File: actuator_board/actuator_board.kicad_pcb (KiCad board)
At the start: 2 copper layers, 26.7 x 37.1 mm, 28 parts, among them J1 Conn_01x10_Socket, J2 Conn_01x02_Socket, Q1 Q_NMOS_GSD, Q2 Q_NMOS_GSD, Q3 Q_NMOS_GSD, Q4 Q_NMOS_GSD, Q5 Q_NMOS_GSD, U1 113991054, U8 STLQ015M33R

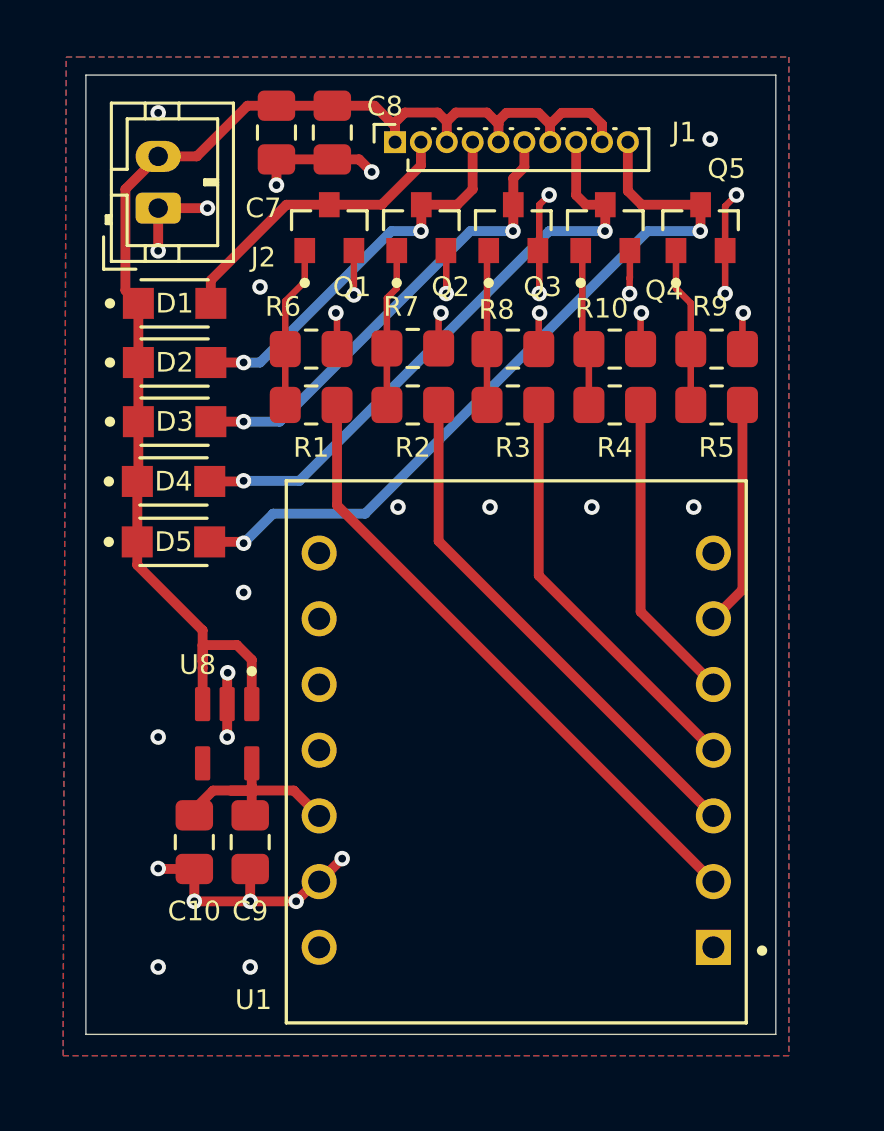
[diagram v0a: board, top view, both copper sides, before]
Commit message: Fixed actuator board and revised magnetometer board
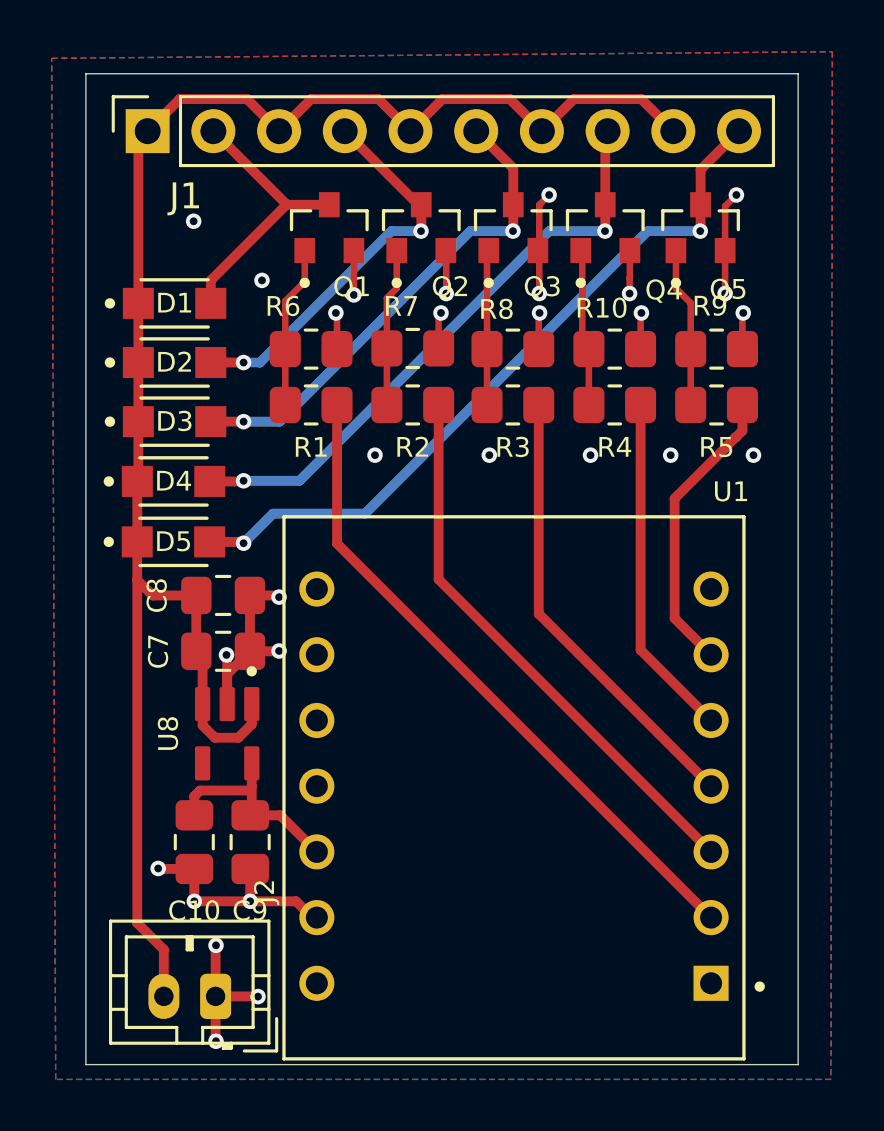
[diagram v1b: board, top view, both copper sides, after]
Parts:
- J1: footprint Connector_PinSocket_1.00mm:PinSocket_1x10_P1.00mm_Vertical -> Connector_PinSocket_2.54mm:PinSocket_1x10_P2.54mm_Vertical
- moved J2 30.6 mm to (134.3, 112.0), turned to 180 degrees
- moved C7 20.2 mm to (134.6, 98.7), turned to 0 degrees
- moved C8 18.4 mm to (134.6, 96.5), turned to 0 degrees
- moved J1 9.57 mm to (131.7, 78.6)
- moved U1 1.39 mm to (145.8, 103.9)
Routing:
- net +V_{BATT}: track 51.4 -> 69.8 mm
- net Net-(U1-D5): track 8.73 -> 11.3 mm
- net GND: track 41.3 -> 43.1 mm, vias 34 -> 28
- net /MOTOR5-: track 29.9 -> 28.5 mm
- net Net-(U1-D3): track 16.1 -> 17.5 mm
- net Net-(U1-D2): track 20.3 -> 21.6 mm
- net Net-(U1-D1): track 24.5 -> 25.8 mm
- net Net-(U1-D4): track 12.0 -> 13.3 mm
- net /MOTOR1-: track 11.8 -> 10.7 mm
- net /MOTOR3-: track 18.4 -> 19.2 mm
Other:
- board size 26.7 x 37.1 mm -> 27.5 x 38.3 mm

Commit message: updates
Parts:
- moved J2 0.15 mm to (134.1, 112.0)
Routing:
- net GND: track 43.1 -> 42.0 mm, vias 28 -> 32
- net /MOTOR2-: track 15.4 -> 16.3 mm

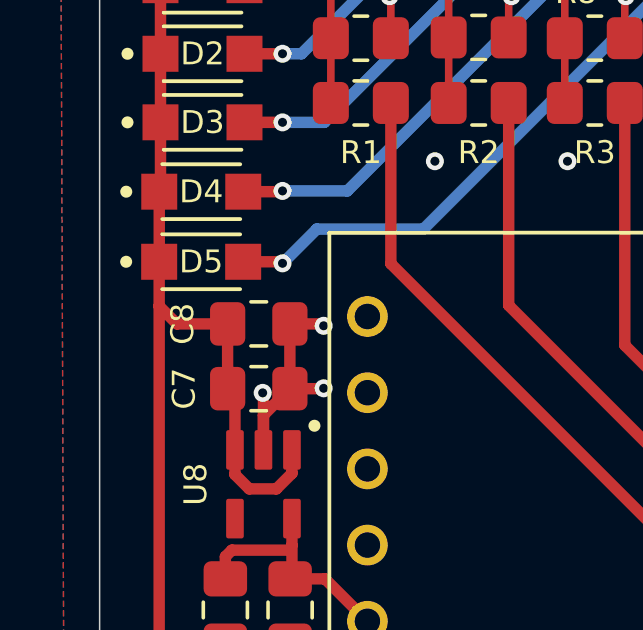
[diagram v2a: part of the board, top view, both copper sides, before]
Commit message: Re-layout of sensor control board
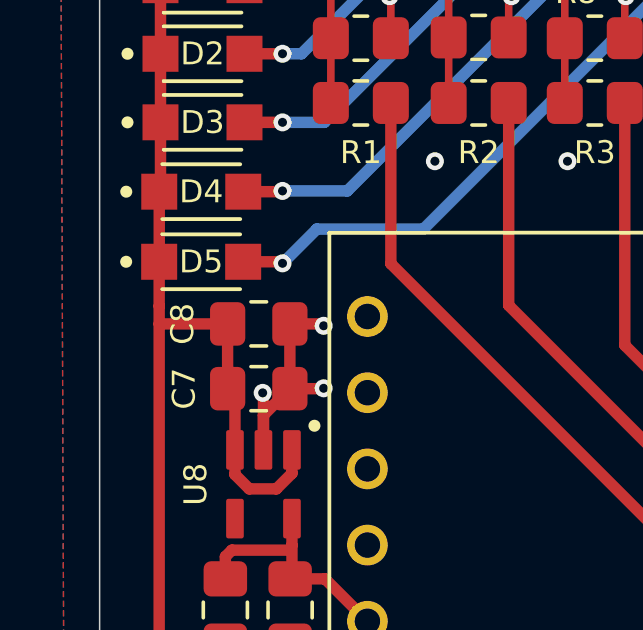
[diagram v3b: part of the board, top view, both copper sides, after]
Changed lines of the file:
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@@
+	)
+	(segment
+		(start 131.2705 96.5073)
+		(end 133.5532 96.5073)
+		(width 0.381)
+		(layer "F.Cu")
+		(net 2)
 	)
 	(segment
@@
 	)
 	(segment
-		(start 131.2705 95.9137)
-		(end 131.8641 96.5073)
-		(width 0.381)
-		(layer "F.Cu")
-		(net 2)
-	)
-	(segment
 		(start 134.273908 102.0064)
 		(end 133.797 101.529492)
@@
 		(width 0.381)
 		(layer "F.Cu")
-		(net 2)
-	)
-	(segment
-		(start 131.8641 96.5073)
-		(end 133.5532 96.5073)
-		(width 0.381)
-		(layer "F.Cu")

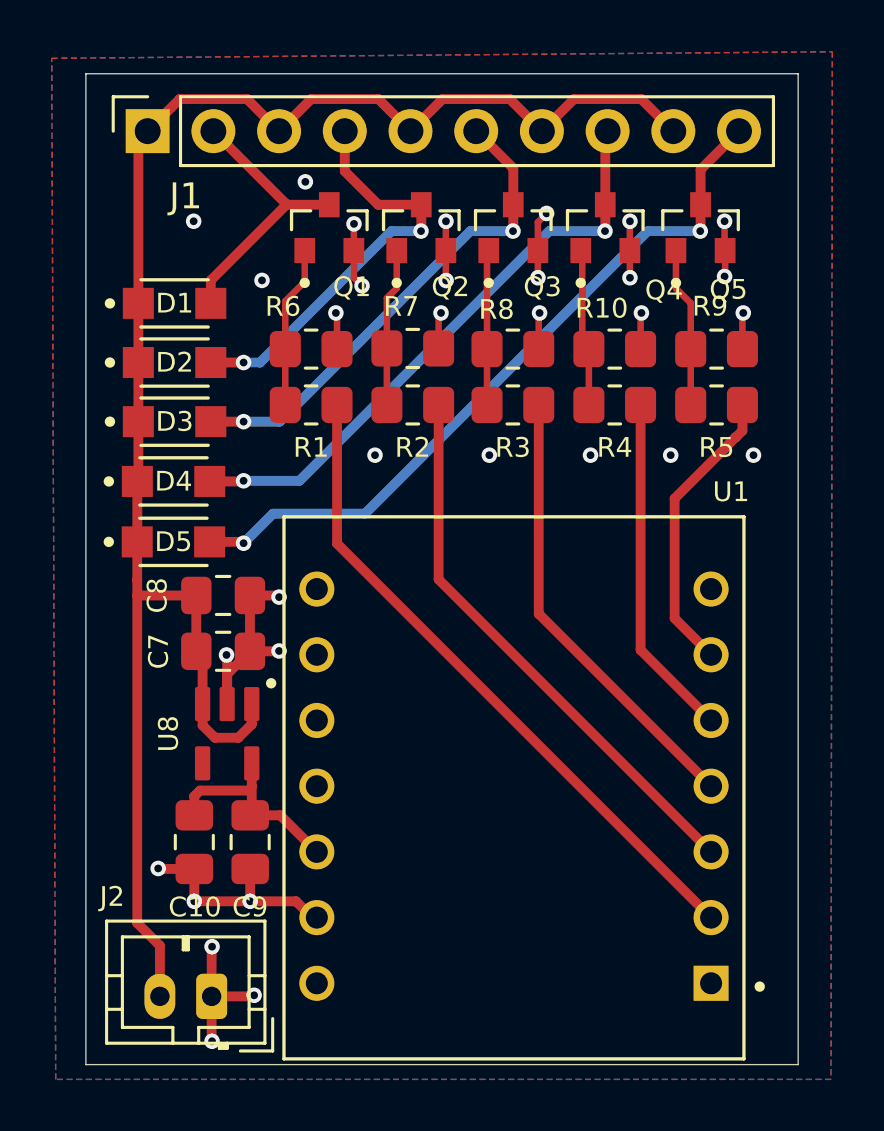
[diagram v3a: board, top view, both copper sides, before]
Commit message: Fixed battery issues, removed LDOs
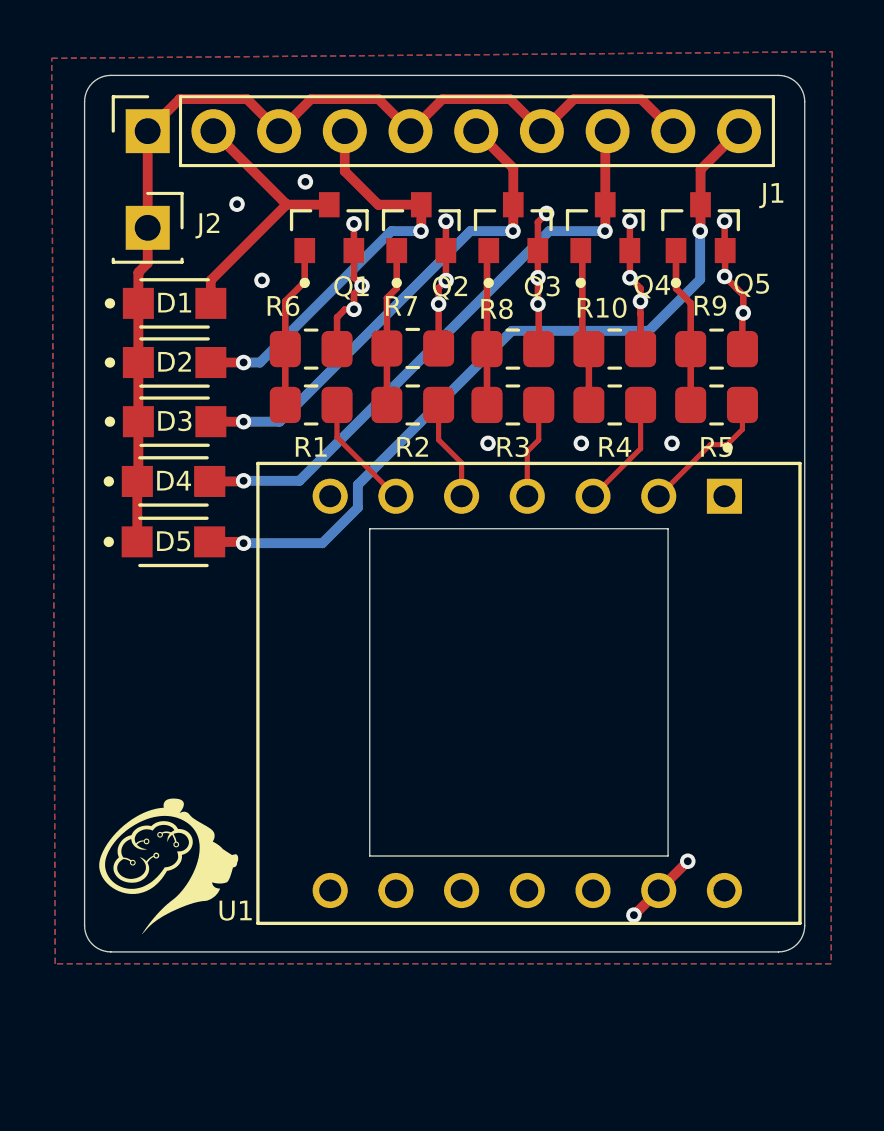
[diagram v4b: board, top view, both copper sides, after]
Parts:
- removed C10, C7: 10uF, Capacitor_SMD:C_0805_2012Metric_Pad1.18x1.45mm_HandSolder
- removed C8, C9: 1uF, Capacitor_SMD:C_0805_2012Metric_Pad1.18x1.45mm_HandSolder
- removed U8: STLQ015M33R, STLQ015M33R:SOT95P280X145-5N
- added G***: LOGO, Electric-Feel:ntablogo, F.Cu at (132.6, 106.9)
- J2: value Conn_01x02_Socket -> Conn_01x01_Socket; footprint Connector_JST:JST_PH_B2B-PH-K_1x02_P2.00mm_Vertical -> Connector_PinSocket_2.54mm:PinSocket_1x01_P2.54mm_Vertical
- moved J2 29.8 mm to (131.7, 82.3), turned to 0 degrees
- moved U1 3.70 mm to (146.4, 100.3), turned to -90 degrees
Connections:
- J2 pad 1: GND -> +V_{BATT}
- R1 pad 1: Net-(U1-D1) -> Net-(U1-D5)
- R2 pad 1: Net-(U1-D2) -> Net-(U1-D4)
- R4 pad 1: Net-(U1-D4) -> Net-(U1-D2)
- R5 pad 1: Net-(U1-D5) -> Net-(U1-D1)
- U1 pad 12: +3V3 -> unconnected-(U1-VCC_3V3-Pad12)
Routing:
- net +V_{BATT}: track 69.5 -> 41.1 mm
- net Net-(U1-D1): track 25.8 -> 5.25 mm
- net Net-(U1-D2): track 21.6 -> 4.29 mm
- net Net-(U1-D3): track 17.5 -> 3.71 mm
- net GND: track 42.0 -> 29.5 mm, vias 32 -> 23
- net Net-(U1-D4): track 13.3 -> 3.90 mm
- net +3V3: track 8.22 -> 0.00 mm
- net Net-(U1-D5): track 11.3 -> 4.47 mm
- net /MOTOR5-: track 28.5 -> 30.1 mm
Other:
- board size 27.5 x 38.3 mm -> 27.8 x 33.9 mm

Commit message: Final version
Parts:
- moved G*** 0.22 mm to (132.8, 106.9)
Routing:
- net GND: track 29.5 -> 31.5 mm, vias 23 -> 33
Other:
- outline, holes or cut-outs redrawn
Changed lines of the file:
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@@
 		(at 146.4126 100.2927 -90)
 		(property "Reference" "U1"
-			(at 8.4193 11.3354 180)
+			(at -4.0267 11.6402 180)
 			(layer "F.SilkS")
 			(effects
@@
 	(footprint "Electric-Feel:ntablogo"
 		(layer "F.Cu")
-		(at 132.552847 106.94175)
+		(at 132.7658 106.9086)
 		(property "Reference" "G***"
 			(at 0 0 0)
@@
 	)
 	(gr_arc
-		(start 129.2352 77.4192)
-		(mid 129.53278 76.70078)
-		(end 130.2512 76.4032)
+		(start 155.6004 76.3778)
+		(mid 156.678031 76.824169)
+		(end 157.1244 77.9018)
 		(stroke
 			(width 0.05)
@@
 	)
 	(gr_arc
-		(start 157.0736 109.2708)
-		(mid 156.77602 109.98922)
-		(end 156.0576 110.2868)
+		(start 130.81 110.2614)
+		(mid 129.732369 109.815031)
+		(end 129.286 108.7374)
 		(stroke
 			(width 0.05)
@@
 		(layer "Edge.Cuts")
 	)
-	(gr_arc
-		(start 156.0576 76.4032)
-		(mid 156.77602 76.70078)
-		(end 157.0736 77.4192)
+	(gr_line
+		(start 130.81 76.3778)
+		(end 155.6004 76.3778)
 		(stroke
 			(width 0.05)
@@
 	)
 	(gr_line
-		(start 156.0576 110.2868)
-		(end 130.2512 110.2868)
+		(start 155.6004 110.2614)
+		(end 130.81 110.2614)
 		(stroke
 			(width 0.05)
@@
 	)
 	(gr_arc
-		(start 130.2512 110.2868)
-		(mid 129.53278 109.98922)
-		(end 129.2352 109.2708)
+		(start 129.286 77.9018)
+		(mid 129.732369 76.824169)
+		(end 130.81 76.3778)
 		(stroke
 			(width 0.05)
@@
 	)
 	(gr_line
-		(start 130.2512 76.4032)
-		(end 156.0576 76.4032)
+		(start 129.286 108.7374)
+		(end 129.286 77.9018)
 		(stroke
 			(width 0.05)
@@
 	)
 	(gr_line
-		(start 129.2352 109.2708)
-		(end 129.2352 77.4192)
+		(start 157.1244 77.9018)
+		(end 157.1244 108.7374)
 		(stroke
 			(width 0.05)
@@
 		(layer "Edge.Cuts")
 	)
-	(gr_line
-		(start 157.0736 77.4192)
-		(end 157.0736 109.2708)
+	(gr_arc
+		(start 157.1244 108.7374)
+		(mid 156.678031 109.815031)
+		(end 155.6004 110.2614)
 		(stroke
 			(width 0.05)
@@
 	)
 	(segment
+		(start 150.114 108.8136)
+		(end 150.5204 108.8136)
+		(width 0.381)
+		(layer "F.Cu")
+		(net 1)
+	)
+	(segment
 		(start 143.2015 84.3243)
 		(end 143.210858 84.333658)
@@
 	)
 	(segment
+		(start 152.3492 108.8136)
+		(end 151.4483 107.9127)
+		(width 0.381)
+		(layer "F.Cu")
+		(net 1)
+	)
+	(segment
 		(start 146.7915 85.2727)
 		(end 146.7915 86.9835)
@@
 	)
 	(segment
+		(start 151.4483 107.9127)
+		(end 151.4291 107.9127)
+		(width 0.381)
+		(layer "F.Cu")
+		(net 1)
+	)
+	(segment
 		(start 139.6492 85.4456)
 		(end 139.3034 85.4456)
@@
 		(end 146.7612 84.2264)
 		(width 0.254)
+		(layer "F.Cu")
+		(net 1)
+	)
+	(segment
+		(start 151.4213 107.9127)
+		(end 151.4291 107.9127)
+		(width 0.381)
 		(layer "F.Cu")
 		(net 1)
@@
 	)
 	(segment
-		(start 151.4213 107.9127)
-		(end 150.4696 108.8644)
+		(start 150.5204 108.8136)
+		(end 151.4213 107.9127)
 		(width 0.381)
 		(layer "F.Cu")
@@
 	)
 	(segment
-		(start 151.4291 107.9127)
-		(end 151.4213 107.9127)
+		(start 152.7048 108.8136)
+		(end 152.3492 108.8136)
 		(width 0.381)
 		(layer "F.Cu")
@@
 	)
 	(via
+		(at 154.4828 97.4598)
+		(size 0.6)
+		(drill 0.3)
+		(layers "F.Cu" "B.Cu")
+		(free yes)
+		(net 1)
+	)
+	(via
 		(at 139.6492 85.4456)
 		(size 0.6)
@@
 	)
 	(via
-		(at 150.4696 108.8644)
-		(size 0.6)
-		(drill 0.3)
-		(layers "F.Cu" "B.Cu")
+		(at 150.114 108.8136)
+		(size 0.6)
+		(drill 0.3)
+		(layers "F.Cu" "B.Cu")
+		(net 1)
+	)
+	(via
+		(at 154.4574 100.1522)
+		(size 0.6)
+		(drill 0.3)
+		(layers "F.Cu" "B.Cu")
+		(free yes)
 		(net 1)
 	)
@@
 	)
 	(via
+		(at 137.795 105.3592)
+		(size 0.6)
+		(drill 0.3)
+		(layers "F.Cu" "B.Cu")
+		(free yes)
+		(net 1)
+	)
+	(via
 		(at 139.959658 84.536858)
 		(size 0.6)
@@
 	)
 	(via
+		(at 152.7048 108.8136)
+		(size 0.6)
+		(drill 0.3)
+		(layers "F.Cu" "B.Cu")
+		(net 1)
+	)
+	(via
+		(at 154.4574 102.6668)
+		(size 0.6)
+		(drill 0.3)
+		(layers "F.Cu" "B.Cu")
+		(free yes)
+		(net 1)
+	)
+	(via
 		(at 144.8308 90.6272)
 		(size 0.6)
@@
 	)
 	(via
+		(at 137.8204 97.4852)
+		(size 0.6)
+		(drill 0.3)
+		(layers "F.Cu" "B.Cu")
+		(free yes)
+		(net 1)
+	)
+	(via
 		(at 146.7612 85.2424)
 		(size 0.6)
@@
 	)
 	(via
+		(at 154.4828 95.0722)
+		(size 0.6)
+		(drill 0.3)
+		(layers "F.Cu" "B.Cu")
+		(free yes)
+		(net 1)
+	)
+	(via
 		(at 142.9213 85.2424)
 		(size 0.6)
@@
 	)
 	(via
+		(at 137.795 100.1776)
+		(size 0.6)
+		(drill 0.3)
+		(layers "F.Cu" "B.Cu")
+		(free yes)
+		(net 1)
+	)
+	(via
 		(at 151.9428 90.6272)
 		(size 0.6)
@@
 	)
 	(via
+		(at 137.795 102.6922)
+		(size 0.6)
+		(drill 0.3)
+		(layers "F.Cu" "B.Cu")
+		(free yes)
+		(net 1)
+	)
+	(via
 		(at 153.9748 82.042)
 		(size 0.6)
@@
 		(net 1)
 	)
+	(via
+		(at 154.4574 105.3338)
+		(size 0.6)
+		(drill 0.3)
+		(layers "F.Cu" "B.Cu")
+		(free yes)
+		(net 1)
+	)
